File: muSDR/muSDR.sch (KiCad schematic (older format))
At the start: 89 parts, among them J10 AudioJack3, J11 Conn_01x02_Male, J12 AudioJack3, J2 Conn_01x02_Male, J3 Conn_01x02_Male, J4 Conn_01x02_Male, J5 Conn_01x02_Male, J6 Conn_02x03_Odd_Even, J9 Conn_01x04_Male, P1 BNC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

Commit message: Added U6, finished smoother, tried to fix digikey-kicad-library submodule.
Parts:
- removed J6: Conn_02x03_Odd_Even, symbol Connector_Generic:Conn_02x03_Odd_Even
- removed L2: 300uH, symbol Device:L
- removed R2: R, symbol Device:R
- added J1: Conn_01x02_Male, Pin_Headers:Pin_Header_Straight_1x02_Pitch2.54mm, symbol Connector:Conn_01x02_Male
- added U6: MC78M05_TO252, TO_SOT_Packages_SMD:TO-252-2, symbol Regulator_Linear:MC78M05_TO252
- Q1: symbol dk_Transistors-Bipolar-BJT-Single:MMBT2222A-TP -> muSDR-rescue:MMBT2222A-TP-dk_Transistors-Bipolar-BJT-Single
- U5: value LT6231 -> LT6231 (or LM4562)
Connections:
- net +4.3V: now also J1.1 (Pin_1)
- net +5V: now also C4.1, L1.1, J1.2 (Pin_2), U6.3 (VO)
- net GND: now also U6.2 (GND)
- net V_IN: now also C1.1, D1.3 (K), U6.1 (VI); no longer C4.1
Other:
- note added: "Reverse\npolarity\nprotection"
- note added: "Smoother\ndisable jumper\n(makes +4.3V \nall +5V)"
- note removed: "ATMEGA328\nprogramming\nheader/test\nport"
- moved on the sheet: C4, D1, J2, TP1

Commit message: Added another pair of holes for a band pass filter hack.
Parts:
- added J6: Conn_01x02_Male, Pin_Headers:Pin_Header_Straight_1x02_Pitch2.54mm, symbol Connector:Conn_01x02_Male
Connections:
- net at J4.2 (Pin_2), P1.1 (In): now also J6.2 (Pin_2)
- net at C6.2, J4.1 (Pin_1): now also J6.1 (Pin_1)
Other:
- note added: "Don't popluate\nJ6. It is to solder\na BP filter hack."
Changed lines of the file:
@@
 Text Notes 8800 2800 0    50   ~ 0
 Jumper for ground \nloop mediation
-Text Notes 3050 2400 0    50   ~ 0
+Text Notes 2450 2650 0    50   ~ 0
 Jumper for \nground loop \nmediation
 Text Notes 850  4650 0    50   ~ 0
@@
 Text Notes 750  1400 0    50   ~ 0
 Reverse\npolarity\nprotection
+$Comp
+L Connector:Conn_01x02_Male J6
+U 1 1 5F23035F
+P 3400 2150
+F 0 "J6" V 3508 2194 50  0000 L CNN
+F 1 "Conn_01x02_Male" H 3508 2240 50  0001 C CNN
+F 2 "Pin_Headers:Pin_Header_Straight_1x02_Pitch2.54mm" H 3400 2150 50  0001 C CNN
+F 3 "~" H 3400 2150 50  0001 C CNN
+	1    3400 2150
+	0    1    -1   0
+$EndComp
+Connection ~ 3400 1950
+Connection ~ 3300 1950
+Text Notes 3050 2400 0    50   ~ 0
+Don't popluate\nJ6.  It is to solder\na BP filter hack.
 $EndSCHEMATC

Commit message: finished footprints and schematic "done"
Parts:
- J10: footprint (none) -> digikey-footprints:Headphone_Jack_2.5mm_SJ1-3523N
- J9: footprint (none) -> Pin_Headers:Pin_Header_Straight_1x04_Pitch2.54mm
- L1: footprint (none) -> Inductors_SMD:L_7.3x7.3_H4.5
- P1: footprint (none) -> Connectors_TE-Connectivity:BNC_Socket_TYCO-AMP_LargePads
- R1, R10, R11, R12, R13, R14, R15, R16, R17, R18, R19, R20, R21, R22, R23, R3, R4, R5, R6, R7, R8, R9, RV1: footprint (none) -> Resistors_SMD:R_0805
- SW1, SW2: footprint (none) -> Buttons_Switches_SMD:SW_SPST_B3S-1000
- TP1, TP10, TP11, TP12, TP13, TP14, TP15, TP16, TP17, TP2, TP3, TP4, TP5, TP6, TP7, TP8, TP9: footprint (none) -> Connectors:PINTST
- Y1: footprint (none) -> Crystals:Crystal_SMD_Abracon_ABM8G-4pin_3.2x2.5mm
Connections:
- net MISO: no longer names the net of A1.15 (D12(PB4))
- net MOSI: no longer names the net of A1.14 (D11(PB3))
- net RESET: no longer names the net of A1.3 (~RESET)
- net RESET: no longer U4.NRST (RESET)
- net SCK: no longer names the net of A1.16 (D13(PB5))
- no-connect marks 19 -> 24

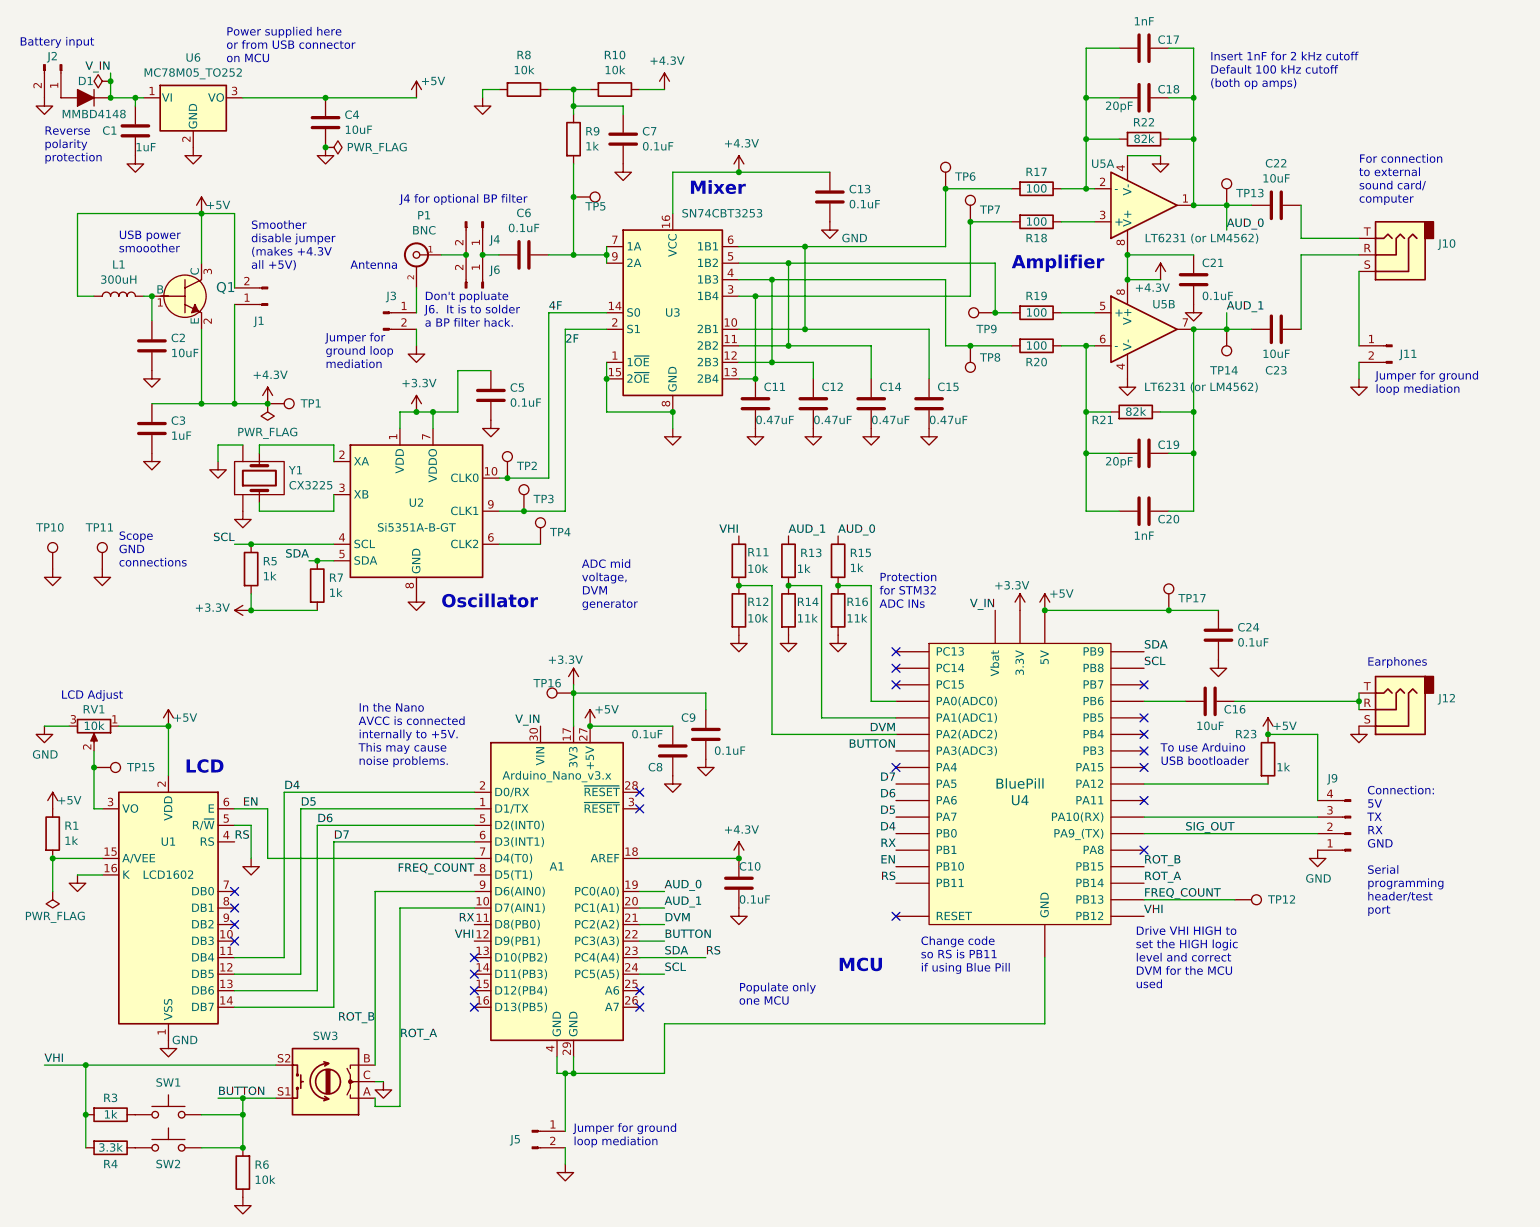
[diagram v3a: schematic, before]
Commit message: Fixed several footprints, and started placing parts....
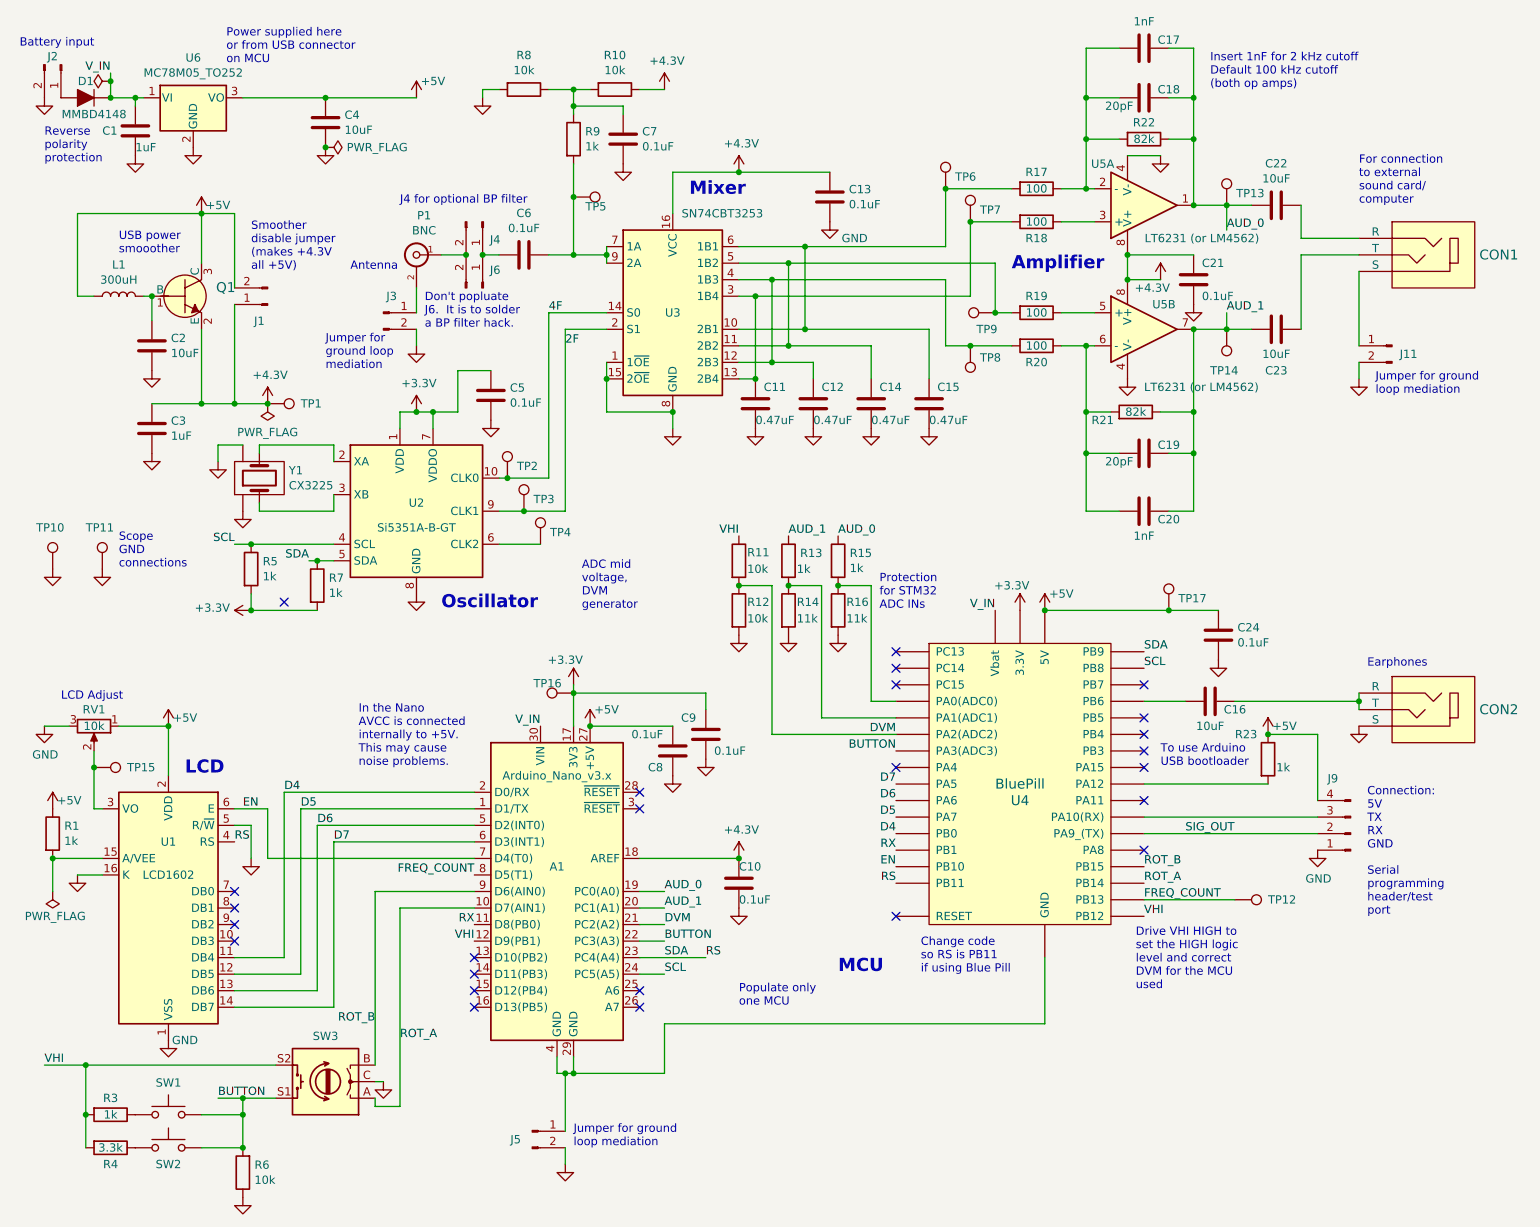
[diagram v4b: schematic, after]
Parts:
- removed J10, J12: AudioJack3, digikey-footprints:Headphone_Jack_2.5mm_SJ1-3523N, symbol Connector:AudioJack3
- added CON1, CON2: SJ1-3523N, digikey-footprints:Headphone_Jack_2.5mm_SJ1-3523N, symbol dk_Barrel-Audio-Connectors:SJ1-3523N
- A1: footprint Module:Arduino_Nano -> Modules:Arduino_Nano
- RV1: footprint Resistors_SMD:R_0805 -> Potentiometers:Potentiometer_Trimmer_ACP_CA6h_Vertical
- SW1, SW2: footprint Buttons_Switches_SMD:SW_SPST_B3S-1000 -> Buttons_Switches_THT:SW_PUSH_6mm_h4.3mm
- SW3: footprint digikey-footprints:Rotary_Encoder_Switched_PEC11R -> SMA:Rotary_Encoder_Switched_PEC11R
- U2: footprint Package_SO:MSOP-10_3x3mm_P0.5mm -> Housings_SSOP:MSOP-10_3x3mm_Pitch0.5mm
- U3: footprint Housings_SOIC:SOIC-14_3.9x8.7mm_Pitch1.27mm -> Housings_SOIC:SOIC-16_3.9x9.9mm_Pitch1.27mm
- U4: footprint blue_pill:BLUEPILL -> BP:BLUEPILL
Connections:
- net GND: now also CON2.1 (S)
- net at C22.1: now also CON1.3 (R)
- net at C23.1: now also CON1.2 (T)
- net at J11.1 (Pin_1): now also CON1.1 (S)
- net at C16.1: now also CON2.2 (T), CON2.3 (R)
- no-connect marks 24 -> 25
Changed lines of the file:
@@
 F 0 "U3" H 4550 2300 50  0000 C CNN
 F 1 "SN74CBT3253" H 4850 2900 50  0000 C CNN
-F 2 "Housings_SOIC:SOIC-14_3.9x8.7mm_Pitch1.27mm" H 4550 2300 50  0001 C CNN
+F 2 "Housings_SOIC:SOIC-16_3.9x9.9mm_Pitch1.27mm" H 4550 2300 50  0001 C CNN
 F 3 "http://www.ti.com/lit/gpn/sn74cbt3253" H 4550 2300 50  0001 C CNN
 	1    4550 2300
@@
 F 0 "U2" H 3000 3550 50  0000 C CNN
 F 1 "Si5351A-B-GT" H 3000 3400 50  0000 C CNN
-F 2 "Package_SO:MSOP-10_3x3mm_P0.5mm" H 3000 2700 50  0001 C CNN
+F 2 "Housings_SSOP:MSOP-10_3x3mm_Pitch0.5mm" H 3000 2700 50  0001 C CNN
 F 3 "https://www.silabs.com/documents/public/data-sheets/Si5351-B.pdf" H 2650 3400 50  0001 C CNN
 	1    3000 3500
@@
 F 0 "RV1" V 950 4800 50  0000 C CNN
 F 1 "10k" V 1050 4800 50  0000 C CNN
-F 2 "Resistors_SMD:R_0805" H 1050 4800 50  0001 C CNN
+F 2 "Potentiometers:Potentiometer_Trimmer_ACP_CA6h_Vertical" H 1050 4800 50  0001 C CNN
 F 3 "~" H 1050 4800 50  0001 C CNN
 	1    1050 4800
@@
 F 0 "SW3" H 2450 6675 50  0000 C CNN
 F 1 "Rotary_Encoder_Switch" H 2450 6674 50  0001 C CNN
-F 2 "digikey-footprints:Rotary_Encoder_Switched_PEC11R" H 2300 7110 50  0001 C CNN
-F 3 "~" H 2450 7210 50  0001 C CNN
+F 2 "SMA:Rotary_Encoder_Switched_PEC11R" H 2300 7110 50  0001 C CNN
+F 3 "https://www.bourns.com/docs/product-datasheets/pec11r.pdf" H 2450 7210 50  0001 C CNN
 	1    2450 6950
 	-1   0    0    1
@@
 	0    1    1    0
 $EndComp
-$Comp
-L Connector:AudioJack3 J10
-U 1 1 5F1D69D0
-P 8900 1950
-F 0 "J10" H 8620 1883 50  0000 R CNN
-F 1 "AudioJack3" H 8620 1974 50  0001 R CNN
-F 2 "digikey-footprints:Headphone_Jack_2.5mm_SJ1-3523N" H 8900 1950 50  0001 C CNN
-F 3 "~" H 8900 1950 50  0001 C CNN
-	1    8900 1950
-	-1   0    0    1
-$EndComp
 Wire Wire Line
 	8350 2400 8350 1950
@@
 F 0 "A1" H 3850 5950 50  0000 C CNN
 F 1 "Arduino_Nano_v3.x" H 3850 6500 50  0000 C CNN
-F 2 "Module:Arduino_Nano" H 3850 5800 50  0001 C CIN
+F 2 "Modules:Arduino_Nano" H 3850 5800 50  0001 C CIN
 F 3 "http://www.mouser.com/pdfdocs/Gravitech_Arduino_Nano3_0.pdf" H 3850 5800 50  0001 C CNN
 	1    3850 5800
@@
 F 0 "SW1" H 1500 7343 50  0000 C CNN
 F 1 "SW_Push" H 1500 7344 50  0001 C CNN
-F 2 "Buttons_Switches_SMD:SW_SPST_B3S-1000" H 1500 7350 50  0001 C CNN
+F 2 "Buttons_Switches_THT:SW_PUSH_6mm_h4.3mm" H 1500 7350 50  0001 C CNN
 F 3 "~" H 1500 7350 50  0001 C CNN
 	1    1500 7150
@@
 F 0 "SW2" H 1500 7250 50  0000 C CNN
 F 1 "SW_Push" H 1500 7544 50  0001 C CNN
-F 2 "Buttons_Switches_SMD:SW_SPST_B3S-1000" H 1500 7550 50  0001 C CNN
+F 2 "Buttons_Switches_THT:SW_PUSH_6mm_h4.3mm" H 1500 7550 50  0001 C CNN
 F 3 "~" H 1500 7550 50  0001 C CNN
 	1    1500 7350
@@
 	0    1    1    0
 $EndComp
-$Comp
-L Connector:AudioJack3 J12
-U 1 1 5F95F929
-P 8900 4700
-F 0 "J12" H 8620 4633 50  0000 R CNN
-F 1 "AudioJack3" H 8620 4724 50  0001 R CNN
-F 2 "digikey-footprints:Headphone_Jack_2.5mm_SJ1-3523N" H 8900 4700 50  0001 C CNN
-F 3 "https://www.cui.com/product/resource/digikeypdf/sj1-352xn_series.pdf" H 8900 4700 50  0001 C CNN
-	1    8900 4700
-	-1   0    0    1
-$EndComp
 Wire Wire Line
 	7950 4650 8700 4650
@@
 F 0 "U4" H 6650 5050 60  0000 C CNN
 F 1 "BluePill" H 6650 5150 60  0000 C CNN
-F 2 "blue_pill:BLUEPILL" H 6550 5900 60  0001 C CNN
+F 2 "BP:BLUEPILL" H 6550 5900 60  0001 C CNN
 F 3 "https://stm32-base.org/boards/STM32F103C8T6-Blue-Pill.html" H 6550 5900 60  0001 C CNN
 	1    6650 5150
@@
 NoConn ~ 5900 5950
 NoConn ~ 4350 5300
+NoConn ~ 2200 4050
+$Comp
+L dk_Barrel-Audio-Connectors:SJ1-3523N CON2
+U 1 1 5F160AB4
+P 9100 4700
+F 0 "CON2" H 8772 4700 60  0000 R CNN
+F 1 "SJ1-3523N" H 8772 4647 60  0001 R CNN
+F 2 "digikey-footprints:Headphone_Jack_2.5mm_SJ1-3523N" H 9300 4900 60  0001 L CNN
+F 3 "https://www.cui.com/product/resource/digikeypdf/sj1-352xn_series.pdf" H 9300 5000 60  0001 L CNN
+F 4 "CP1-3523N-ND" H 9300 5100 60  0001 L CNN "Digi-Key_PN"
+F 5 "SJ1-3523N" H 9300 5200 60  0001 L CNN "MPN"
+F 6 "Connectors, Interconnects" H 9300 5300 60  0001 L CNN "Category"
+F 7 "Barrel - Audio Connectors" H 9300 5400 60  0001 L CNN "Family"
+F 8 "https://www.cui.com/product/resource/digikeypdf/sj1-352xn_series.pdf" H 9300 5500 60  0001 L CNN "DK_Datasheet_Link"
+F 9 "/product-detail/en/cui-inc/SJ1-3523N/CP1-3523N-ND/738689" H 9300 5600 60  0001 L CNN "DK_Detail_Page"
+F 10 "CONN JACK STEREO 3.5MM R/A" H 9300 5700 60  0001 L CNN "Description"
+F 11 "CUI Inc." H 9300 5800 60  0001 L CNN "Manufacturer"
+F 12 "Active" H 9300 5900 60  0001 L CNN "Status"
+	1    9100 4700
+	-1   0    0    -1
+$EndComp
+$Comp
+L dk_Barrel-Audio-Connectors:SJ1-3523N CON1
+U 1 1 5F1644E0
+P 9100 1950
+F 0 "CON1" H 8772 1950 60  0000 R CNN
+F 1 "SJ1-3523N" H 8772 1897 60  0001 R CNN
+F 2 "digikey-footprints:Headphone_Jack_2.5mm_SJ1-3523N" H 9300 2150 60  0001 L CNN
+F 3 "https://www.cui.com/product/resource/digikeypdf/sj1-352xn_series.pdf" H 9300 2250 60  0001 L CNN
+F 4 "CP1-3523N-ND" H 9300 2350 60  0001 L CNN "Digi-Key_PN"
+F 5 "SJ1-3523N" H 9300 2450 60  0001 L CNN "MPN"
+F 6 "Connectors, Interconnects" H 9300 2550 60  0001 L CNN "Category"
+F 7 "Barrel - Audio Connectors" H 9300 2650 60  0001 L CNN "Family"
+F 8 "https://www.cui.com/product/resource/digikeypdf/sj1-352xn_series.pdf" H 9300 2750 60  0001 L CNN "DK_Datasheet_Link"
+F 9 "/product-detail/en/cui-inc/SJ1-3523N/CP1-3523N-ND/738689" H 9300 2850 60  0001 L CNN "DK_Detail_Page"
+F 10 "CONN JACK STEREO 3.5MM R/A" H 9300 2950 60  0001 L CNN "Description"
+F 11 "CUI Inc." H 9300 3050 60  0001 L CNN "Manufacturer"
+F 12 "Active" H 9300 3150 60  0001 L CNN "Status"
+	1    9100 1950
+	-1   0    0    -1
+$EndComp
 $EndSCHEMATC
